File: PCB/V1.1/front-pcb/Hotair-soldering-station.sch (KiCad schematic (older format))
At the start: 28 parts, among them J2 main-board-conn, J3 hot_on, J4 solder_on, SW1 HOTAIR_UP, SW2 HOTAIR_DOWN, SW3 SIRON_UP, SW4 SIRON_DOWN, SW5 SIRON_UP, SW6 SIRON_DOWN, U1 74HC595D

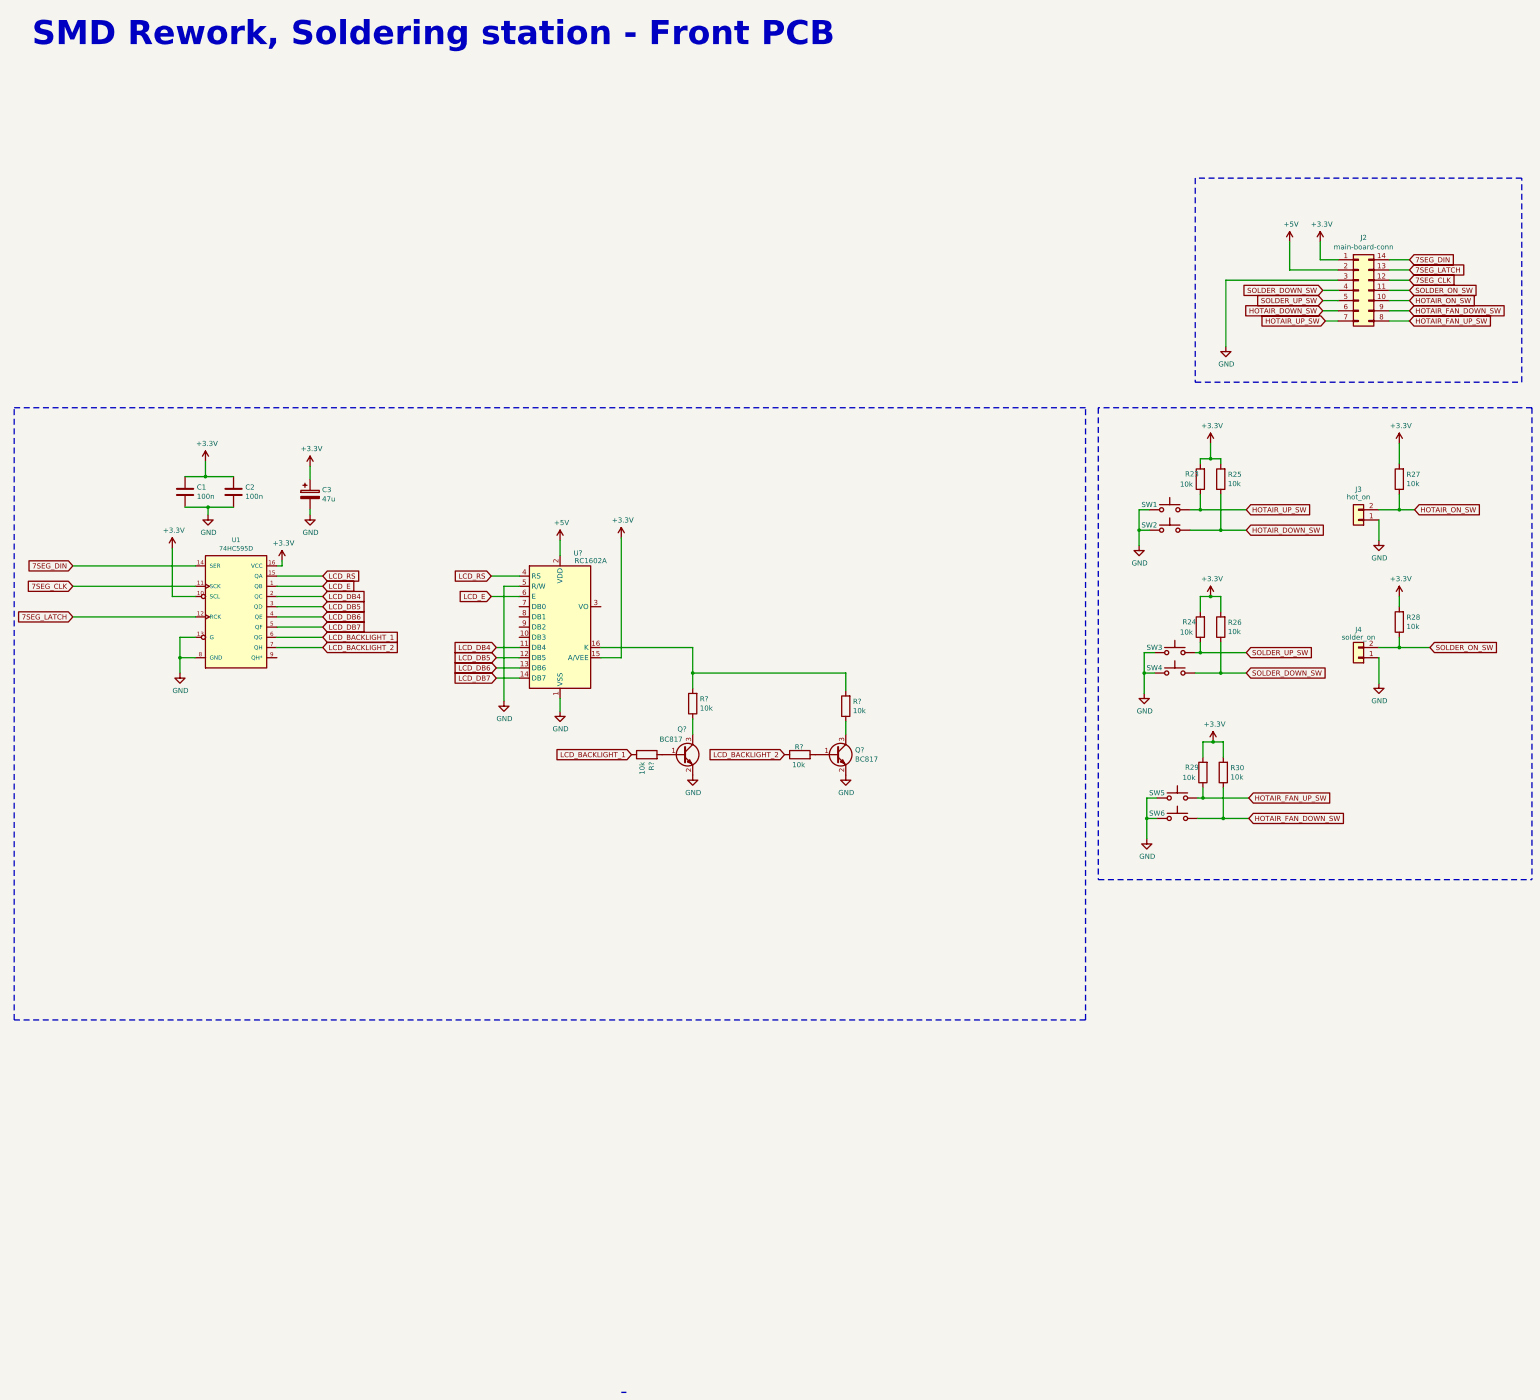
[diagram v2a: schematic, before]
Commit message: Display change to LCD
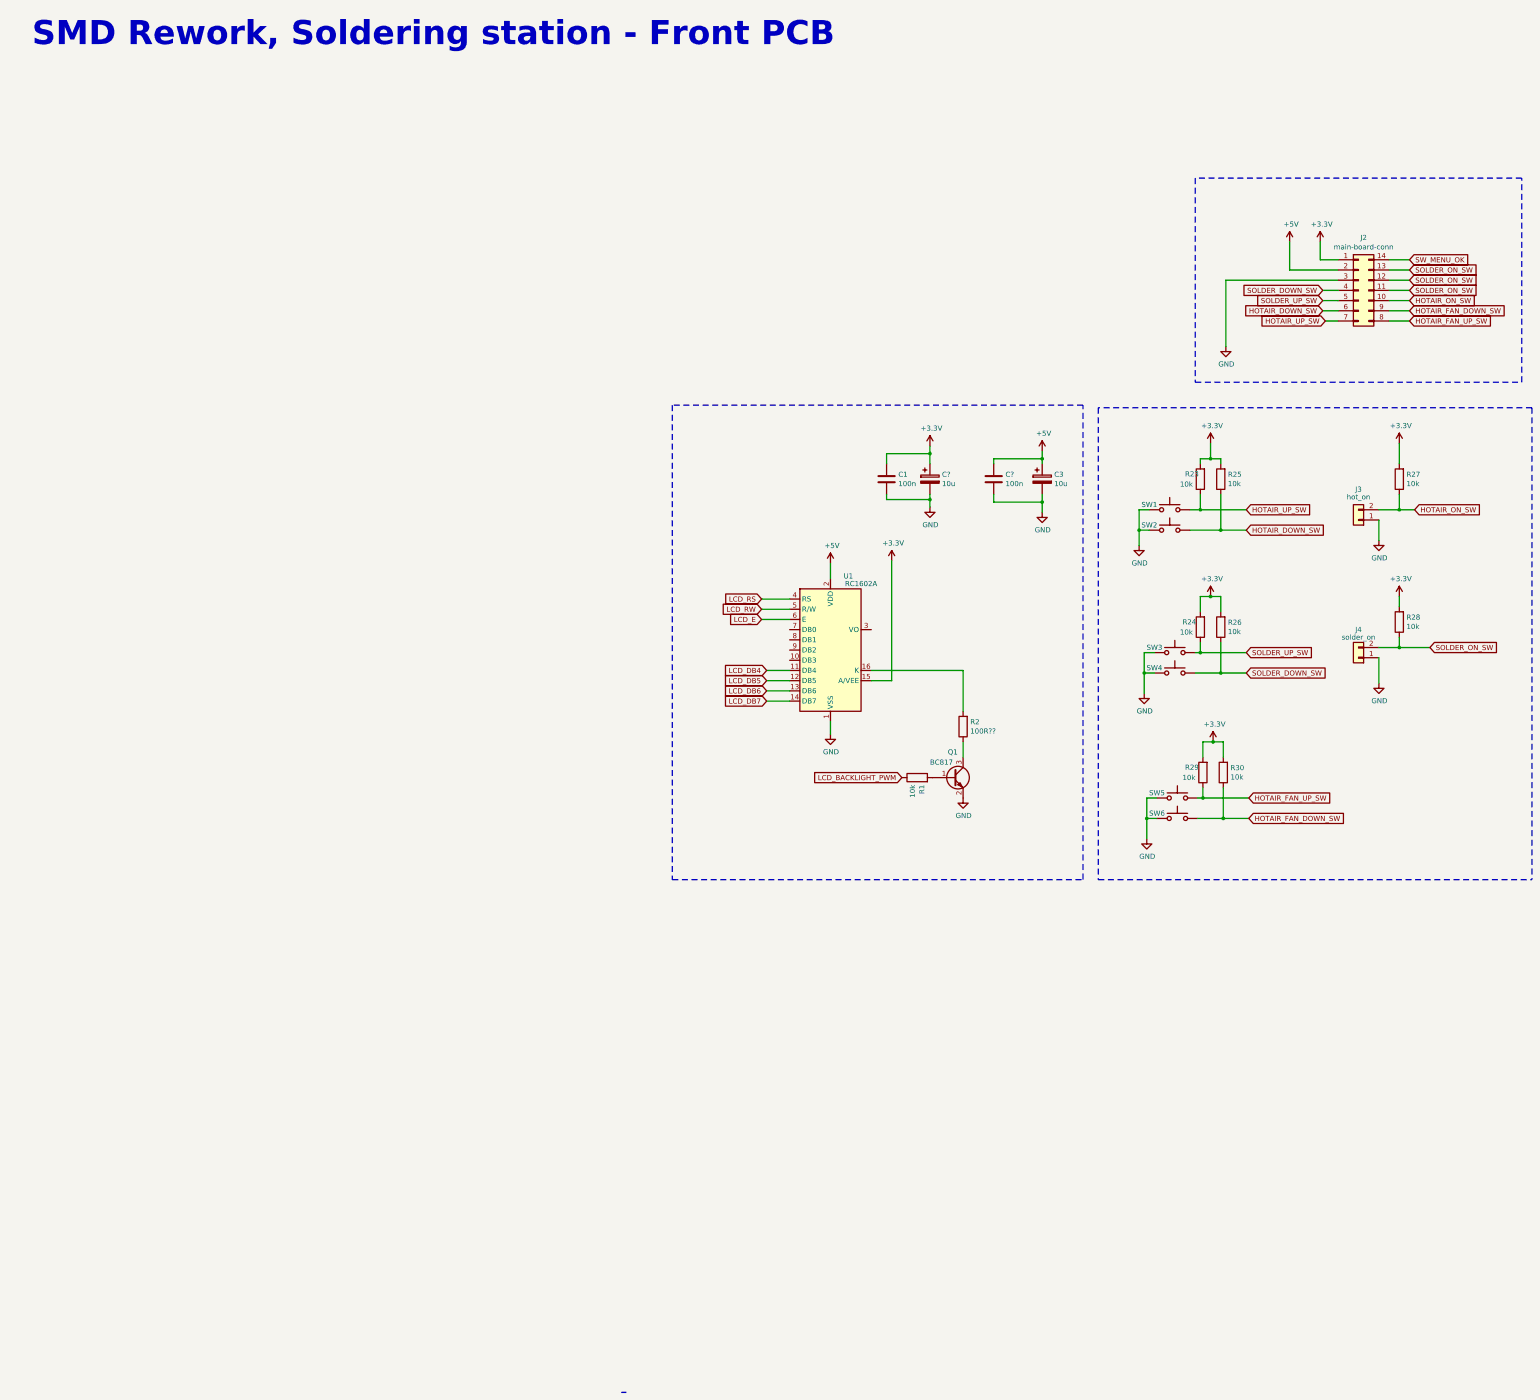
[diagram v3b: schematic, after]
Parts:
- removed C2: 100n, Capacitors:0805, symbol Device:C
- removed Q?: BC817, Package_TO_SOT_SMD:SOT-23, symbol Transistor_BJT:BC817
- removed R? (x2): 10k, Capacitors:0805, symbol Device:R
- removed U1: 74HC595D, Silicon-Standard:SO16, symbol SparkFun-IC-Logic:74HC595D
- added C?: 100n, Capacitors:0805, symbol Device:C
- added C?: 10u, Capacitor_Tantalum_SMD:CP_EIA-3528-21_Kemet-B, symbol Device:CP
- C3: value 47u -> 10u
- R2: renamed from R?; value 10k -> 100R??
- gave numbers to parts that had none: 3
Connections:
- net 7SEG_CLK is gone; now on net SOLDER_ON_SW: J2.12 (Pin_12)
- net 7SEG_LATCH is gone; now on net SOLDER_ON_SW: J2.13 (Pin_13)
- net +3V3: now also C?.1; no longer C3.1
- net +5V: now also C3.1, C?.1
- net GND: now also C?.2, C?.2; no longer U1.5 (R/W)
- net 7SEG_DIN renamed SW_MENU_OK
- net LCD_BACKLIGHT_1 renamed LCD_BACKLIGHT_PWM
- new net LCD_RW: U1.5 (R/W)
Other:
- moved on the sheet: C1, C3, Q1, R1, R2, U1

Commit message: Add front panel menu sw, remove lcd, reorganization of uC pinout
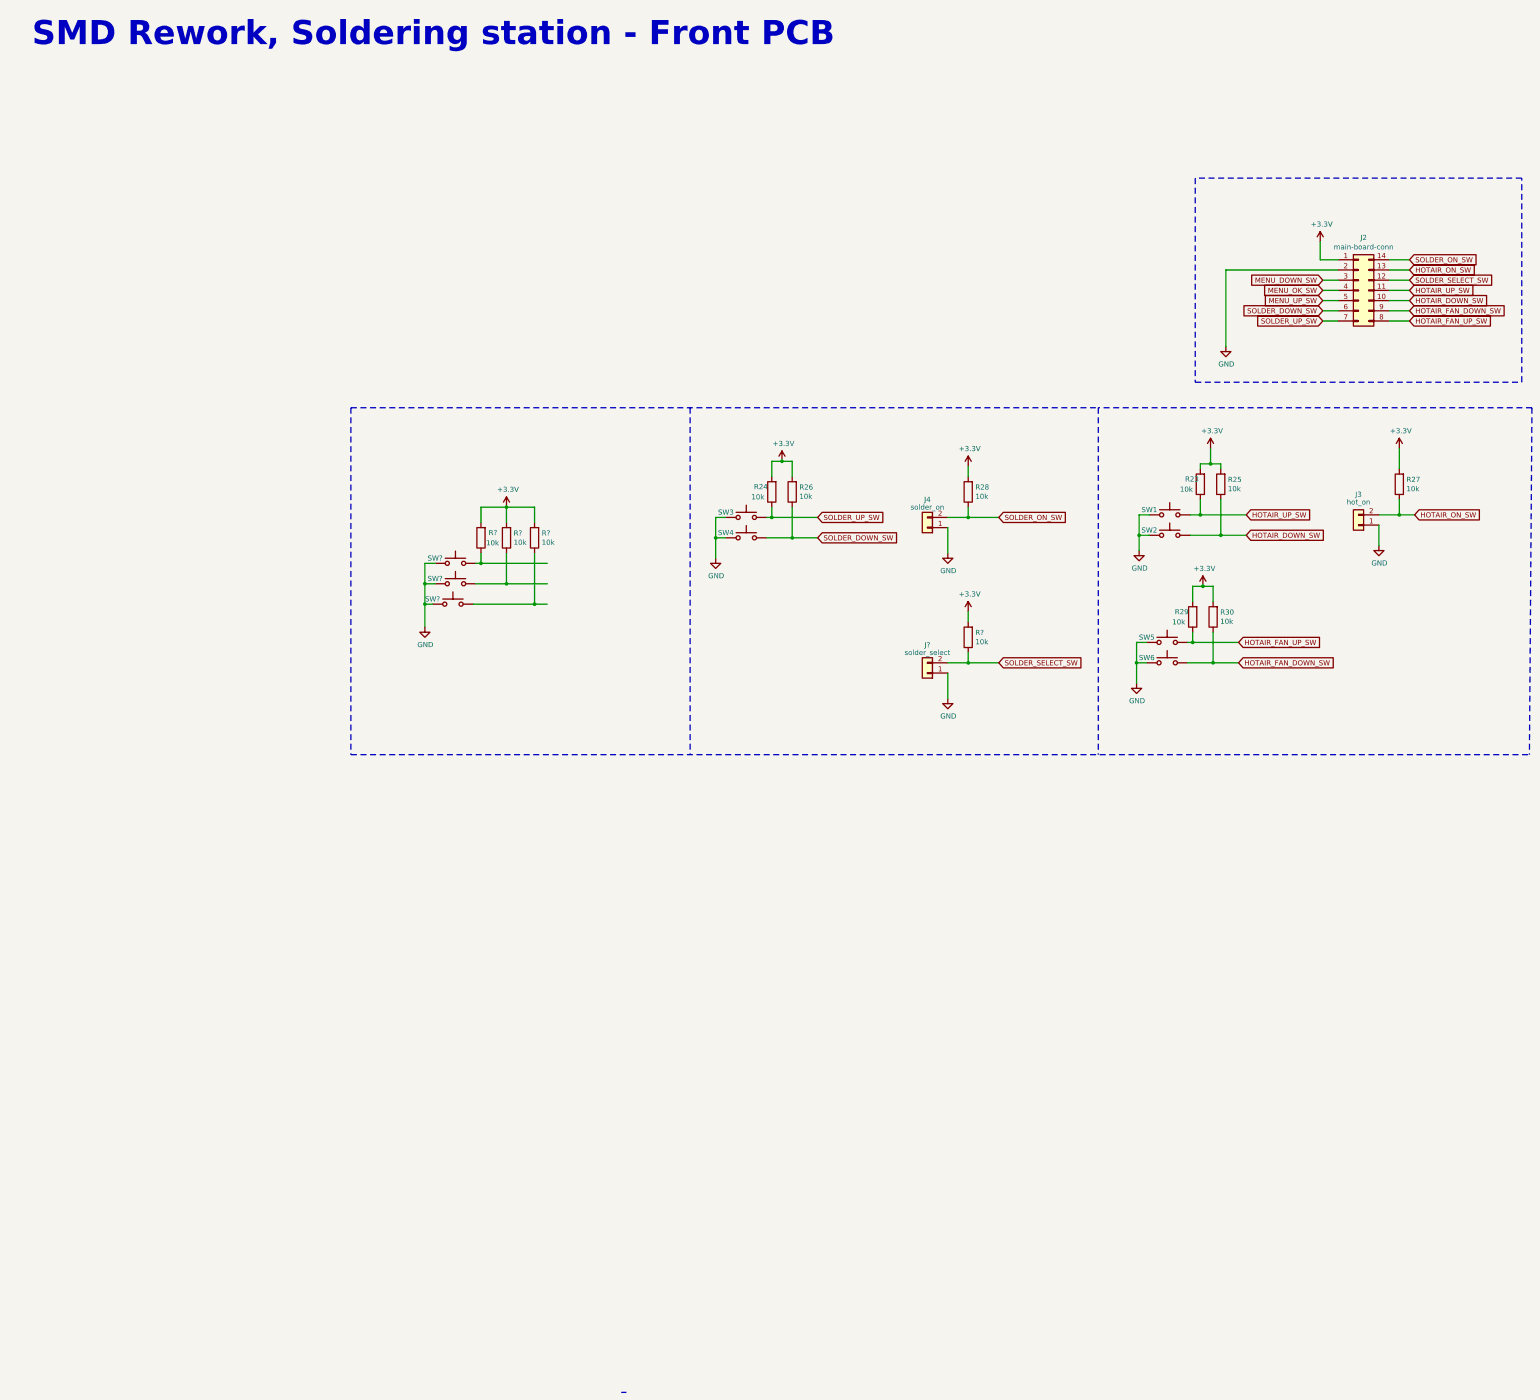
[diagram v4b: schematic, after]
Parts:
- removed C1, C?: 100n, Capacitors:0805, symbol Device:C
- removed C3, C?: 10u, Capacitor_Tantalum_SMD:CP_EIA-3528-21_Kemet-B, symbol Device:CP
- removed Q1: BC817, Package_TO_SOT_SMD:SOT-23, symbol Transistor_BJT:BC817
- removed R1: 10k, Capacitors:0805, symbol Device:R
- removed R2: 100R??, Capacitors:0805, symbol Device:R
- removed U1: RC1602A, Display:RC1602A, symbol Display_Character:RC1602A
- added J?: solder_select, Connector_PinHeader_2.54mm:PinHeader_1x02_P2.54mm_Vertical, symbol Connector_Generic:Conn_01x02
- added R? (x4): 10k, Capacitors:0805, symbol Device:R
- added SW? (x2): SIRON_DOWN, Switches:TACTILE_SWITCH_PTH_12MM, symbol Switch:SW_Push
- added SW?: SIRON_UP, Switches:TACTILE_SWITCH_PTH_12MM, symbol Switch:SW_Push
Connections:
- net labels added: MENU_DOWN_SW, MENU_OK_SW, MENU_UP_SW, SOLDER_SELECT_SW
- net labels removed: +5V, LCD_BACKLIGHT_PWM, LCD_DB4, LCD_DB5, LCD_DB6, LCD_DB7, LCD_E, LCD_RS, LCD_RW, SW_MENU_OK
- wire segments 100 -> 94
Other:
- moved on the sheet: J3, J4, R23, R24, R25, R26, R27, R28, R29, R30, SW1, SW2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
